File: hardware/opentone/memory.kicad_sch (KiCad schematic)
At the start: 30 parts, among them J601 DM3AT-SF-PEJM5, U601 APS6404L-3SQN-SN, U602 TPS22917

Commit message: updated BOM
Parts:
- C601, C606: value 100n -> 100nF
- C602: value 4.7u -> 4.7uF
- C603: value 1u -> 1uF
- C604: value 1n -> 1nF
- C605: value 10u -> 10uF
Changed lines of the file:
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@@
 			)
 		)
-		(property "Value" "100n"
+		(property "Value" "100nF"
 			(at 83.82 49.53 0)
 			(show_name no)
@@
 			)
 		)
-		(property "Value" "100n"
+		(property "Value" "100nF"
 			(at 340.36 57.15 0)
 			(show_name no)
@@
 			)
 		)
-		(property "Value" "10u"
+		(property "Value" "10uF"
 			(at 330.2 57.15 0)
 			(show_name no)
@@
 			)
 		)
-		(property "Value" "1n"
+		(property "Value" "1nF"
 			(at 271.78 77.47 0)
 			(show_name no)
@@
 			)
 		)
-		(property "Value" "1u"
+		(property "Value" "1uF"
 			(at 254 57.15 0)
 			(show_name no)
@@
 			)
 		)
-		(property "Value" "4.7u"
+		(property "Value" "4.7uF"
 			(at 93.98 49.53 0)
 			(show_name no)

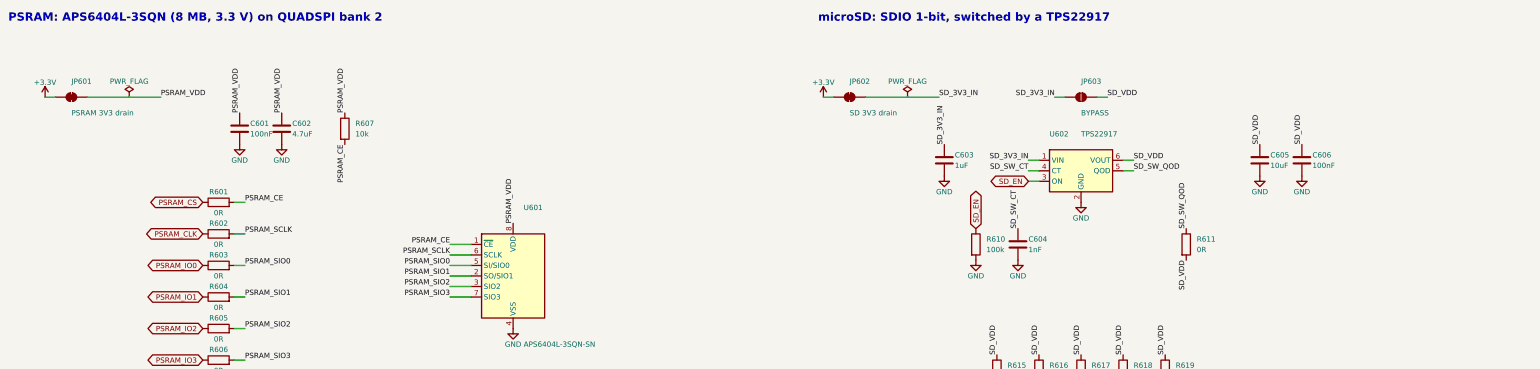
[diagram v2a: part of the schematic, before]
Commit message: started placing the components
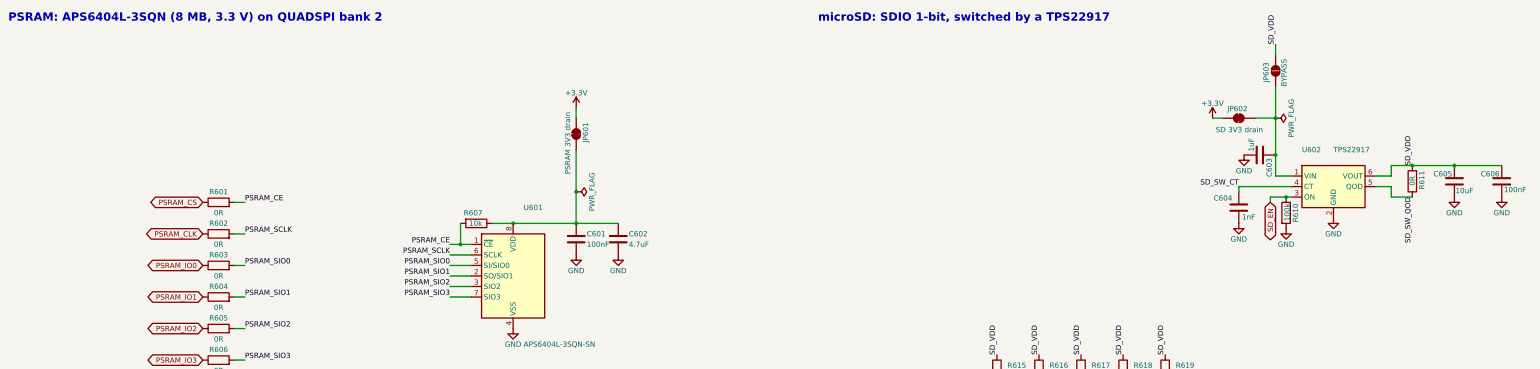
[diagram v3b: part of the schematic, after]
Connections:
- net PSRAM_VDD: no longer names the net of C601.1, C602.1, JP601.2 (B), R607.1, U601.8 (VDD)
- net SD_3V3_IN: no longer names the net of C603.1, JP602.2 (B), JP603.1 (A), U602.1 (VIN)
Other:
- moved on the sheet: C601, C602, C603, C604, C605, C606, JP601, JP602, JP603, R607, R610, R611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
